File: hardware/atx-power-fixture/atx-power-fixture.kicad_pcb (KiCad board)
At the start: 2 copper layers, 32 parts, among them J1 ATX24RH, J2 Screw_Terminal_01x02, J3 BINDING_POST, J4 BINDING_POST, J5 Console FTDI, Q1 DMG2301L, Q2 2N7002, SW1 SW_SPST, SW2 SW_SPST, U1 SSD1306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

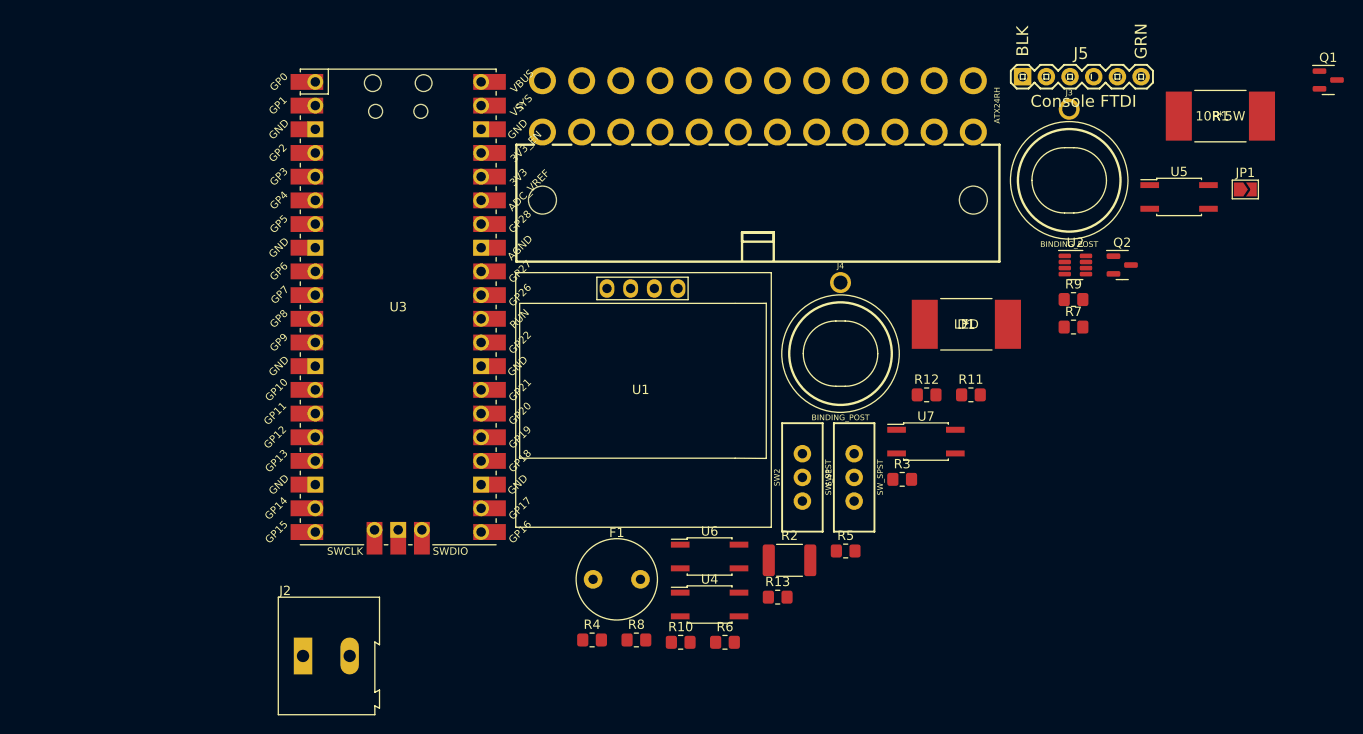
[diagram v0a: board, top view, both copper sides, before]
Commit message: Layout + gerbers for ATX power fixture
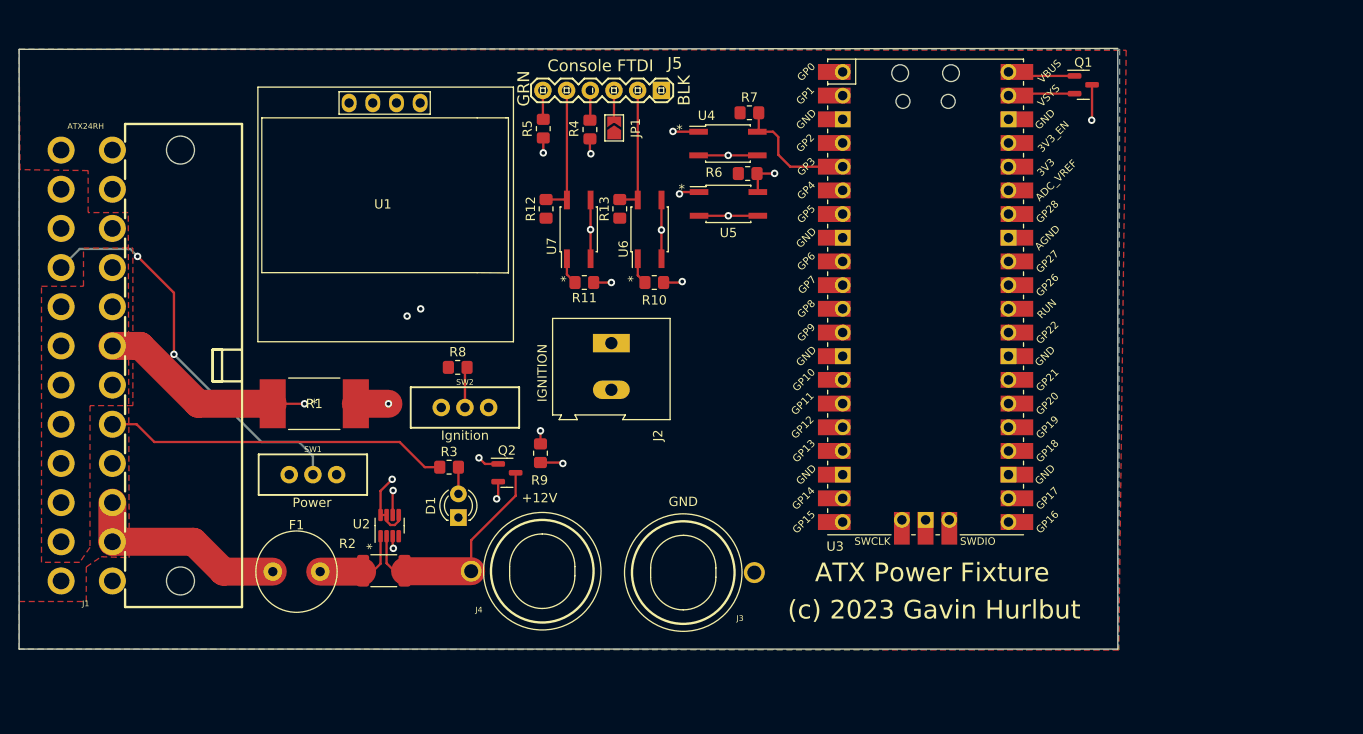
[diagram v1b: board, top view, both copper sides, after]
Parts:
- D1: footprint UltraLibrarian:355010RFT -> LED_THT:LED_D3.0mm
- moved R1 101.9 mm to (118.0, 89.8), turned to 180 degrees
- moved U2 78.7 mm to (126.1, 102.9), turned to 90 degrees
- moved Q2 69.6 mm to (138.7, 97.2)
- moved JP1 68.0 mm to (150.2, 60.2), turned to 90 degrees
- moved J1 67.6 mm to (101.2, 85.7), turned to 90 degrees
- moved R9 59.5 mm to (142.3, 95.1), turned to 90 degrees
- moved J3 59.0 mm to (157.6, 107.9), turned to -90 degrees
- moved D1 58.3 mm to (133.5, 102.0), turned to 90 degrees
- moved SW1 58.0 mm to (117.9, 97.4), turned to -90 degrees
- moved U3 56.6 mm to (183.6, 78.3)
- moved R5 55.7 mm to (142.6, 60.3), turned to -90 degrees
- moved R4 54.7 mm to (147.6, 60.4), turned to -90 degrees
- moved R6 50.3 mm to (164.5, 65.1)
- moved U4 49.5 mm to (162.4, 61.9)
- moved R3 48.6 mm to (132.5, 96.6)
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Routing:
- net +5V: track 0.00 -> 124.2 mm, vias 0 -> 2
- net SCL: track 0.00 -> 96.9 mm, vias 0 -> 2
- net SDA: track 0.00 -> 90.7 mm, vias 0 -> 2
- net Net-(R8-Pad2): track 0.00 -> 68.7 mm
- net Net-(Q2-Pad1): track 0.00 -> 62.0 mm, vias 0 -> 1
- net Net-(J1-Pad16): track 0.00 -> 43.1 mm, vias 0 -> 2
- net LocalTX: track 0.00 -> 39.7 mm, vias 0 -> 1
- net Net-(J1-Pad8): track 0.00 -> 37.0 mm
- net GND: track 0.00 -> 31.4 mm, vias 0 -> 7
- net IGNITION: track 0.00 -> 30.4 mm, vias 0 -> 2
- net LocalRTS: track 0.00 -> 30.0 mm, vias 0 -> 1
- net +12V: track 0.00 -> 24.9 mm
- net +12Vin: track 0.00 -> 22.7 mm
- net Net-(R5-Pad2): track 0.00 -> 19.2 mm, vias 0 -> 2
- net LocalRX: track 0.00 -> 17.3 mm, vias 0 -> 1
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- added copper zone on F.Cu, net +3V3
- added copper zone on F.Cu, net +5V
- added copper zone on B.Cu, net GND
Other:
- board outline added: 117.8 x 64.4 mm
- copper layers 2 -> 4
- board text added: "(c) 2023 Gavin Hurlbut"
- board text added: "ATX Power Fixture"

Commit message: Adding first run of firmware for the ATX board
- displays shunt voltage, bus voltage, current, power
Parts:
- added R9: 10k, Resistor_SMD:R_0805_2012Metric_Pad1.20x1.40mm_HandSolder, B.Cu at (189.9, 101.5)
- renumbered R9 to R10, R10 to R11, R11 to R12, R12 to R13, R13 to R14
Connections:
- U3 pad 24: unconnected-(U3-Pad24) -> GND
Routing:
- net Net-(Q2-Pad1): track 62.0 -> 64.5 mm

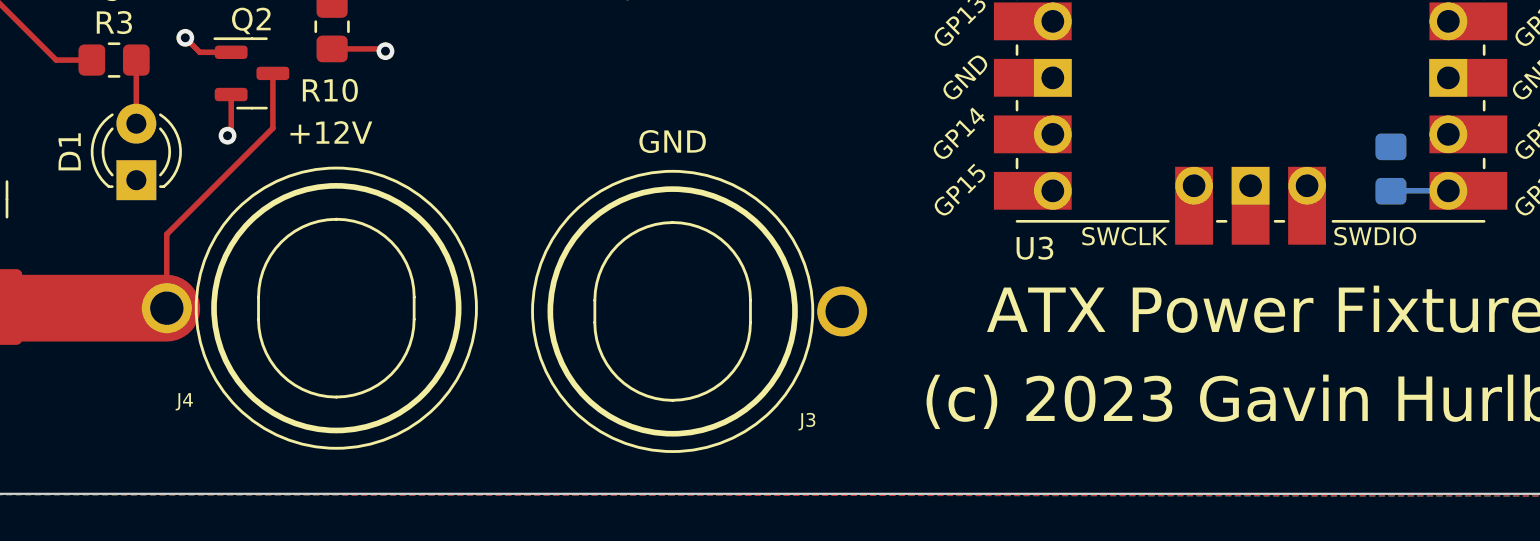
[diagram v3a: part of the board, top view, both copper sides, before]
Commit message: Fixed the binding posts to have HOLES in them
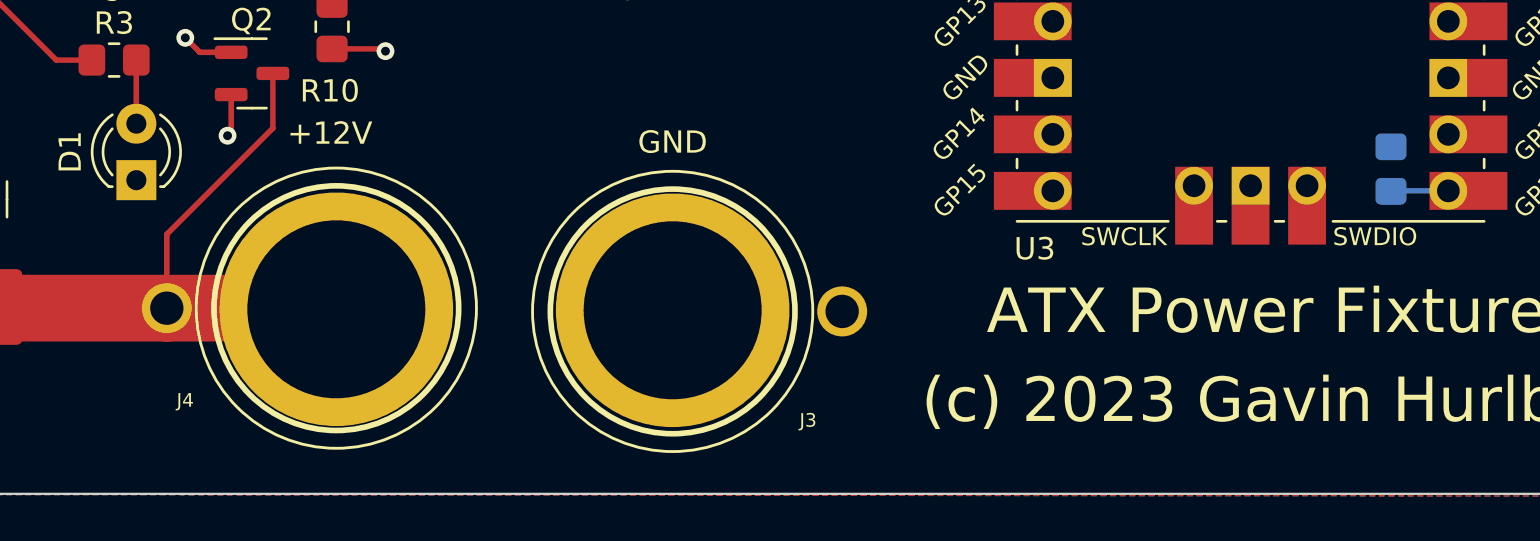
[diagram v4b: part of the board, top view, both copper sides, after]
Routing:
- net +12V: track 24.9 -> 32.5 mm
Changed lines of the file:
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@@
       (effects (font (size 1 1) (thickness 0.15)))
     )
-    (fp_line (start -0.49784 3.49758) (end 0.49784 3.49758) (layer "F.SilkS") (width 0.127))
-    (fp_line (start -0.49784 3.49758) (end 0.49784 3.49758) (layer "F.SilkS") (width 0.127))
-    (fp_line (start 0.49784 -3.49758) (end -0.49784 -3.49758) (layer "F.SilkS") (width 0.127))
-    (fp_line (start 0.49784 -3.49758) (end -0.49784 -3.49758) (layer "F.SilkS") (width 0.127))
-    (fp_arc (start 0.49784 -3.49758) (mid 2.971003 -2.473163) (end 3.99542 0) (layer "F.SilkS") (width 0.127))
-    (fp_arc (start 0.49784 -3.49758) (mid 2.971003 -2.473163) (end 3.99542 0) (layer "F.SilkS") (width 0.127))
-    (fp_arc (start -3.99796 0) (mid -2.972799 -2.474959) (end -0.49784 -3.50012) (layer "F.SilkS") (width 0.127))
-    (fp_arc (start 3.99796 0) (mid 2.972799 2.474959) (end 0.49784 3.50012) (layer "F.SilkS") (width 0.127))
-    (fp_arc (start -0.49784 3.49758) (mid -2.971003 2.473163) (end -3.99542 0) (layer "F.SilkS") (width 0.127))
-    (fp_arc (start -3.99796 0) (mid -2.972799 -2.474959) (end -0.49784 -3.50012) (layer "F.SilkS") (width 0.127))
-    (fp_arc (start -0.49784 3.49758) (mid -2.971003 2.473163) (end -3.99542 0) (layer "F.SilkS") (width 0.127))
-    (fp_arc (start 3.99796 0) (mid 2.972799 2.474959) (end 0.49784 3.50012) (layer "F.SilkS") (width 0.127))
+    (fp_circle (center 0 0) (end 0 -6.2992) (layer "F.SilkS") (width 0.127) (fill none))
     (fp_circle (center 0 0) (end 0 -5.4991) (layer "F.SilkS") (width 0.254) (fill none))
-    (fp_circle (center 0 0) (end 0 -6.2992) (layer "F.SilkS") (width 0.127) (fill none))
     (fp_circle (center 0 0) (end 0 -5.4991) (layer "F.CrtYd") (width 0.127) (fill none))
-    (pad "P$1" thru_hole circle locked (at 0 -7.62 270) (size 2.2479 2.2479) (drill 1.4986) (layers *.Cu *.Mask)
+    (pad "P$1" thru_hole circle (at -0.0508 0 270) (size 10.5 10.5) (drill 8) (layers *.Cu *.Mask)
+      (net 1 "GND") (pinfunction "P$1") (pintype "bidirectional"))
+    (pad "P$1" thru_hole circle (at 0 -7.62 270) (size 2.2479 2.2479) (drill 1.4986) (layers *.Cu *.Mask)
       (net 1 "GND") (pinfunction "P$1") (pintype "bidirectional") (solder_mask_margin 0.1016))
   )
@@
       (effects (font (size 1 1) (thickness 0.15)))
     )
-    (fp_line (start -0.49784 3.49758) (end 0.49784 3.49758) (layer "F.SilkS") (width 0.127))
-    (fp_line (start 0.49784 -3.49758) (end -0.49784 -3.49758) (layer "F.SilkS") (width 0.127))
-    (fp_line (start 0.49784 -3.49758) (end -0.49784 -3.49758) (layer "F.SilkS") (width 0.127))
-    (fp_line (start -0.49784 3.49758) (end 0.49784 3.49758) (layer "F.SilkS") (width 0.127))
-    (fp_arc (start 3.99796 0) (mid 2.972799 2.474959) (end 0.49784 3.50012) (layer "F.SilkS") (width 0.127))
-    (fp_arc (start 0.49784 -3.49758) (mid 2.971003 -2.473163) (end 3.99542 0) (layer "F.SilkS") (width 0.127))
-    (fp_arc (start 0.49784 -3.49758) (mid 2.971003 -2.473163) (end 3.99542 0) (layer "F.SilkS") (width 0.127))
-    (fp_arc (start 3.99796 0) (mid 2.972799 2.474959) (end 0.49784 3.50012) (layer "F.SilkS") (width 0.127))
-    (fp_arc (start -0.49784 3.49758) (mid -2.971003 2.473163) (end -3.99542 0) (layer "F.SilkS") (width 0.127))
-    (fp_arc (start -0.49784 3.49758) (mid -2.971003 2.473163) (end -3.99542 0) (layer "F.SilkS") (width 0.127))
-    (fp_arc (start -3.99796 0) (mid -2.972799 -2.474959) (end -0.49784 -3.50012) (layer "F.SilkS") (width 0.127))
-    (fp_arc (start -3.99796 0) (mid -2.972799 -2.474959) (end -0.49784 -3.50012) (layer "F.SilkS") (width 0.127))
+    (fp_circle (center 0 0) (end 0 -6.2992) (layer "F.SilkS") (width 0.127) (fill none))
     (fp_circle (center 0 0) (end 0 -5.4991) (layer "F.SilkS") (width 0.254) (fill none))
-    (fp_circle (center 0 0) (end 0 -6.2992) (layer "F.SilkS") (width 0.127) (fill none))
     (fp_circle (center 0 0) (end 0 -5.4991) (layer "F.CrtYd") (width 0.127) (fill none))
-    (pad "P$1" thru_hole circle locked (at 0 -7.62 90) (size 2.2479 2.2479) (drill 1.4986) (layers *.Cu *.Mask)
+    (pad "P$1" thru_hole circle (at 0 -7.62 90) (size 2.2479 2.2479) (drill 1.4986) (layers *.Cu *.Mask)
       (net 5 "+12V") (pinfunction "P$1") (pintype "bidirectional") (solder_mask_margin 0.1016))
+    (pad "P$1" thru_hole circle (at -0.0508 0 90) (size 10.5 10.5) (drill 8) (layers *.Cu *.Mask)
+      (net 5 "+12V") (pinfunction "P$1") (pintype "bidirectional"))
   )
   (footprint "UltraLibrarian:355010RFT" (layer "F.Cu")
@@
     (fp_line (start -1 -0.625) (end -1 0.625) (layer "B.Fab") (width 0.1))
     (fp_line (start 1 0.625) (end 1 -0.625) (layer "B.Fab") (width 0.1))
-    (pad "1" smd roundrect (at -1 0 90) (size 1.2 1.4) (layers "B.Cu" "B.Paste" "B.Mask") (roundrect_rratio 0.208333)
+    (pad "1" smd roundrect (at -1 0 90) (size 1.2 1.4) (layers "B.Cu" "B.Paste" "B.Mask") (roundrect_rratio 0.2083333333)
       (net 27 "Net-(Q2-Pad1)") (pintype "passive"))
-    (pad "2" smd roundrect (at 1 0 90) (size 1.2 1.4) (layers "B.Cu" "B.Paste" "B.Mask") (roundrect_rratio 0.208333)
+    (pad "2" smd roundrect (at 1 0 90) (size 1.2 1.4) (layers "B.Cu" "B.Paste" "B.Mask") (roundrect_rratio 0.2083333333)
       (net 1 "GND") (pintype "passive"))
     (model "${KICAD6_3DMODEL_DIR}/Resistor_SMD.3dshapes/R_0805_2012Metric.wrl"
@@
     (effects (font (size 2 2) (thickness 0.3)))
   )
-  (target plus (at 86.4 116) (size 5) (width 0.1) (layer "Edge.Cuts"))
-  (target plus (at 86.4 116) (size 5) (width 0.1) (layer "Edge.Cuts"))
   (segment (start 159.3 69.64) (end 162.44 69.64) (width 0.25) (layer "F.Cu") (net 1))
   (segment (start 159.25 63.17) (end 162.43 63.17) (width 0.25) (layer "F.Cu") (net 1))
@@
   (segment (start 125.8 104) (end 125.8 106.9) (width 0.25) (layer "F.Cu") (net 5))
   (segment (start 126.6 107.7) (end 127.725 107.7) (width 0.25) (layer "F.Cu") (net 5))
+  (segment (start 142.439825 107.753676) (end 142.490625 107.804476) (width 0.25) (layer "F.Cu") (net 5))
   (segment (start 139.6375 97.2) (end 139.6375 99.6625) (width 0.25) (layer "F.Cu") (net 5))
   (segment (start 125.8 106.9) (end 126.6 107.7) (width 0.25) (layer "F.Cu") (net 5))
   (segment (start 134.870625 104.429375) (end 134.870625 107.753676) (width 0.25) (layer "F.Cu") (net 5))
+  (segment (start 134.870625 107.753676) (end 142.439825 107.753676) (width 3) (layer "F.Cu") (net 5))
   (segment (start 144.6 96.1) (end 144.7 96.2) (width 0.25) (layer "F.Cu") (net 6))
   (segment (start 137.7625 98.15) (end 137.7625 99.8375) (width 0.25) (layer "F.Cu") (net 6))

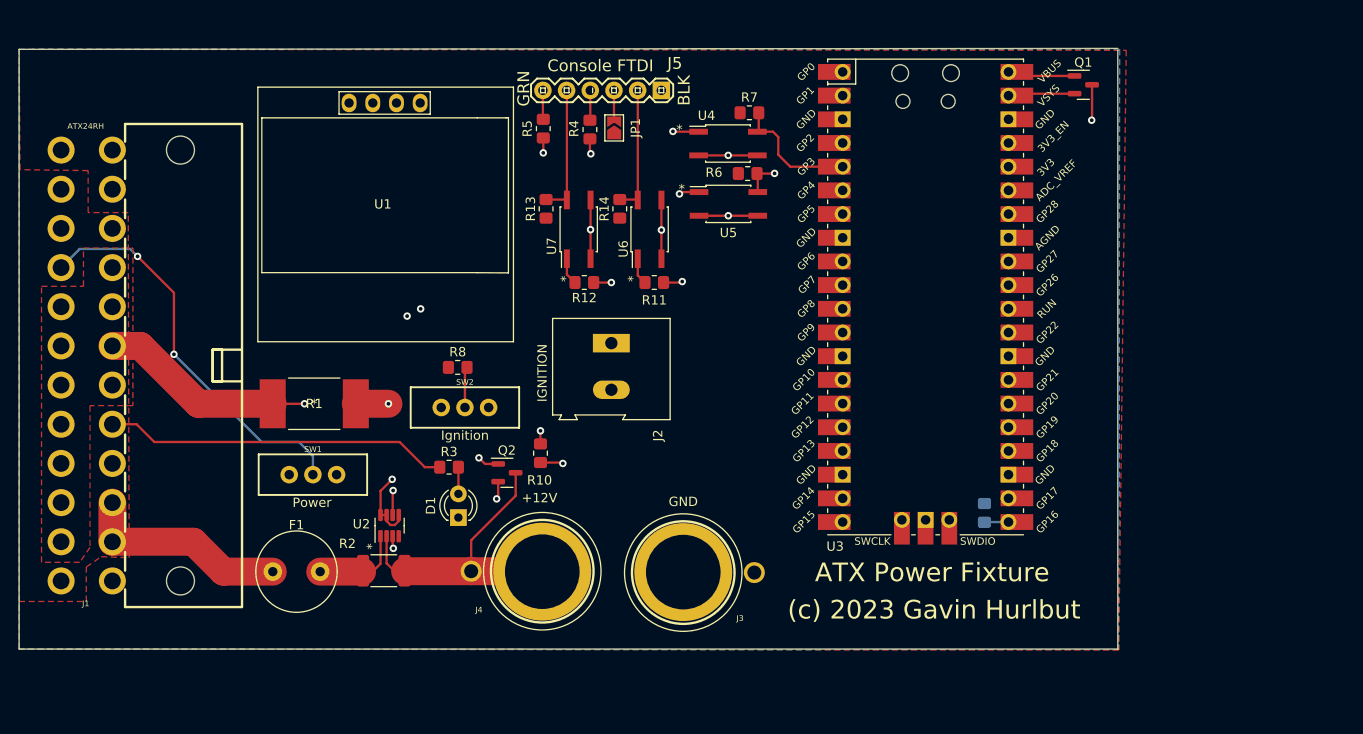
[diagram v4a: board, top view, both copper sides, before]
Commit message: Tried to shrink the board to < 100mm long.  Failed
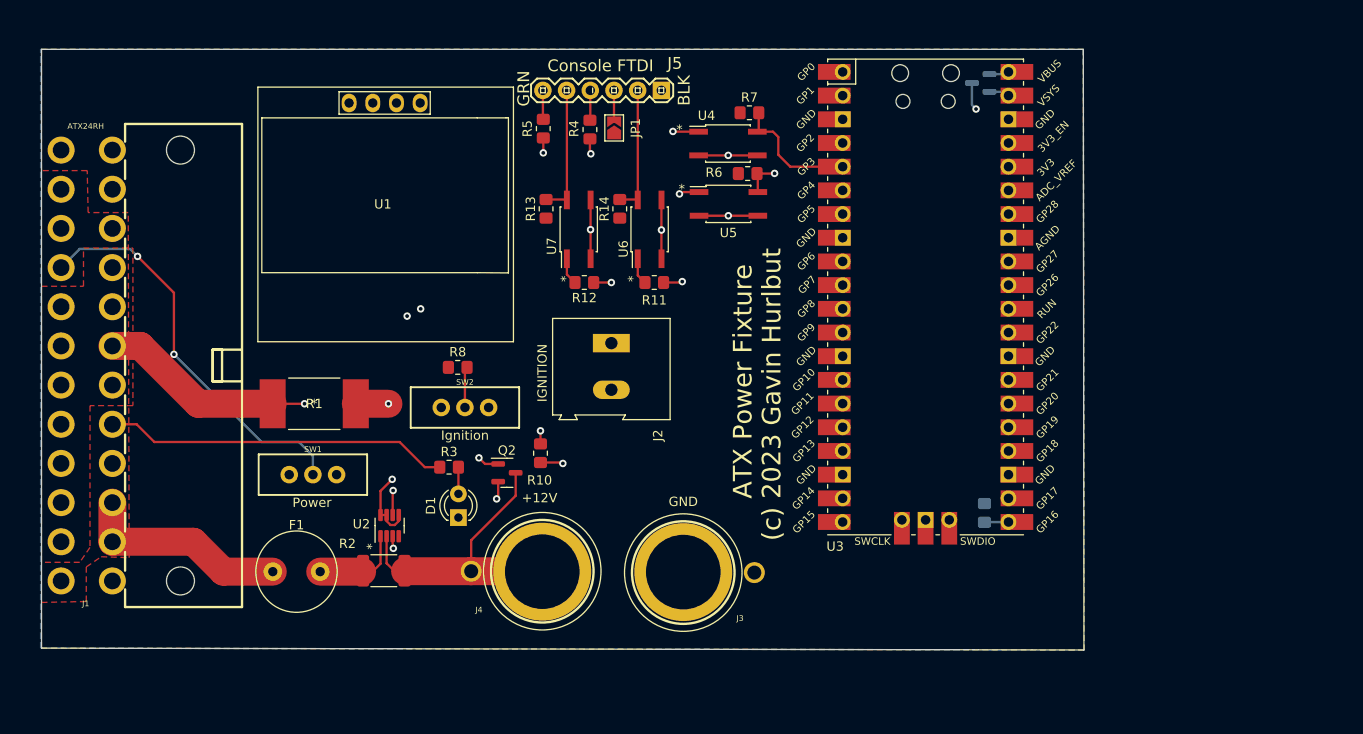
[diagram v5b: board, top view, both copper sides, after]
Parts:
- Q1: moved to B.Cu
- moved Q1 11.0 mm to (189.5, 55.4), turned to 180 degrees
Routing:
- net +5V: track 124.2 -> 116.8 mm
- net /VBUS: track 7.26 -> 2.14 mm
- net /VSYS: track 7.17 -> 2.21 mm
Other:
- board size 117.8 x 64.4 mm -> 111.8 x 64.4 mm
